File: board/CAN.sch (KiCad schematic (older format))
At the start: 4 parts, among them U401 SN65HVD232

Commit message: - changed some more Vcc labels to +3V3 - combined all input connectors into one big connector - changed can transceiver to MAX3051 - removed HV pin from power connector -> divider now on PS board - updated components - startet layout
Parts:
- removed C401: 2.2u, CRF1:SMD-0603_c, symbol C-RESCUE-BLDC_4
- removed R401: NI, CRF1:SMD-0603_r, symbol R-RESCUE-BLDC_4
- removed R402: 10k, CRF1:SMD-0603_r, symbol R-RESCUE-BLDC_4
- removed U401: SN65HVD232, CRF1:SOIC-8-W, symbol MCP2551-I/SN-RESCUE-BLDC_4
- added C9: 100n, Capacitors_SMD:C_0805, symbol C
- added IC1: MAX3051, Housings_SOIC:SOIC-8_3.9x4.9mm_Pitch1.27mm, symbol MAX3051
- added R3: 120R, Resistors_SMD:R_0805, symbol R
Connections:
- net labels added: +3V3
- net labels removed: VCC
- wire segments 8 -> 4
- no-connect marks 1 -> 0
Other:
- note removed: "Propagation delay\nresistor"

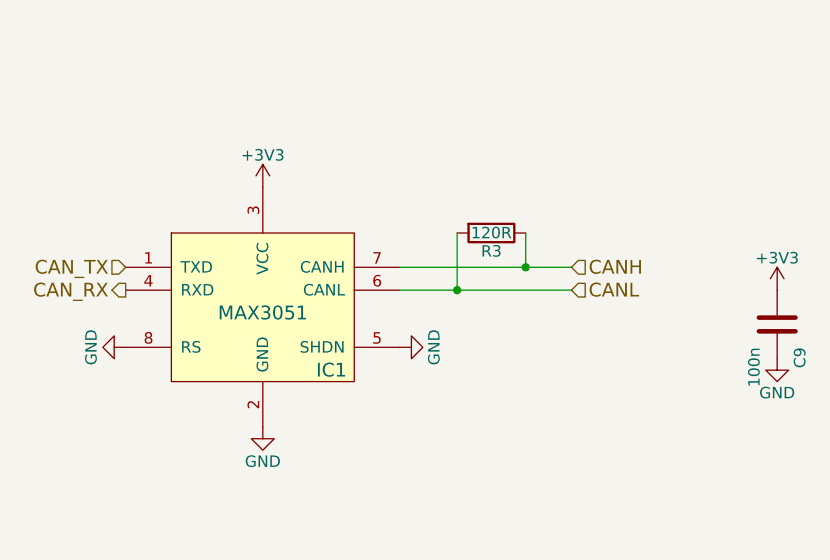
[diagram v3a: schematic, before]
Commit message: - CAN interface isolation
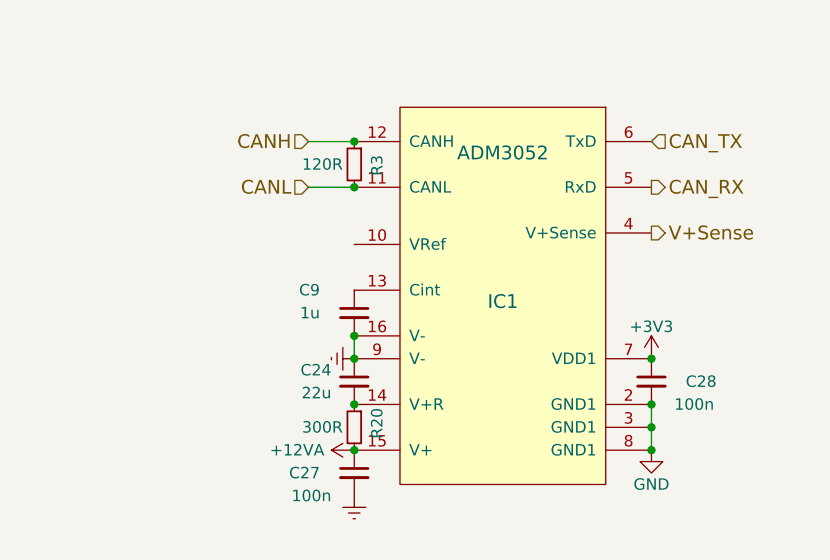
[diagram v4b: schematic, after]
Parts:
- removed C9: 100n, Capacitors_SMD:C_0805, symbol C
- removed IC1: MAX3051, Housings_SOIC:SOIC-8_3.9x4.9mm_Pitch1.27mm, symbol MAX3051
- removed R3: 120R, Resistors_SMD:R_0805, symbol R
- added C24: 22u, Capacitors_SMD:C_0805, symbol C_Small
- added C27, C28: 100n, Capacitors_SMD:C_0805, symbol C_Small
- added C9: 1u, Capacitors_SMD:C_0805, symbol C_Small
- added IC1: ADM3052, Housings_SOIC:SOIC-16_7.5x10.3mm_Pitch1.27mm, symbol ADM3052
- added R20: 300R, Resistors_SMD:R_1206, symbol R_Small
- added R3: 120R, Resistors_SMD:R_0805, symbol R_Small
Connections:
- net +3V3: now also C28.1, IC1.7 (VDD1)
- net CANH: now also IC1.12 (CANH), R3.1
- net CANL: now also IC1.11 (CANL), R3.2
- net CAN_RX: now also IC1.5 (RxD)
- net CAN_TX: now also IC1.6 (TxD)
- net GND: now also C28.2, IC1.2 (GND1), IC1.3 (GND1), IC1.8 (GND1)
- new net: C9.1, IC1.13 (Cint)
- new net: C24.2, IC1.14 (V+R), R20.1
- new net +12VA: C27.1, IC1.15 (V+), R20.2
- new net Earth: C24.1, C27.2, C9.2, IC1.16 (V-), IC1.9 (V-)
- new net V+Sense: IC1.4 (V+Sense)
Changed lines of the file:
@@
 Comment4 ""
 $EndDescr
-Text HLabel 4350 3800 0    60   Output ~ 0
+Text HLabel 6650 3350 2    60   Output ~ 0
 CAN_RX
-Text HLabel 4350 3700 0    60   Input ~ 0
+Text HLabel 6650 3150 2    60   Input ~ 0
 CAN_TX
-Text HLabel 6300 3700 2    60   Input ~ 0
+Text HLabel 5150 3150 0    60   Input ~ 0
 CANH
-Text HLabel 6300 3800 2    60   Input ~ 0
+Text HLabel 5150 3350 0    60   Input ~ 0
 CANL
 $Comp
-L MAX3051 IC1
-U 1 1 57560849
-P 4950 3800
-F 0 "IC1" H 5250 3450 60  0000 C CNN
-F 1 "MAX3051" H 4950 3700 60  0000 C CNN
-F 2 "Housings_SOIC:SOIC-8_3.9x4.9mm_Pitch1.27mm" H 4950 3800 60  0001 C CNN
-F 3 "" H 4950 3800 60  0000 C CNN
-	1    4950 3800
+L ADM3052 IC1
+U 1 1 5759CEA3
+P 6000 3850
+F 0 "IC1" H 6000 3850 60  0000 C CNN
+F 1 "ADM3052" H 6000 4500 60  0000 C CNN
+F 2 "Housings_SOIC:SOIC-16_7.5x10.3mm_Pitch1.27mm" H 6150 3950 60  0001 C CNN
+F 3 "" H 6150 3950 60  0000 C CNN
+	1    6000 3850
+	-1   0    0    -1
+$EndComp
+$Comp
+L C_Small C9
+U 1 1 5759CF39
+P 5350 3900
+F 0 "C9" H 5500 4000 50  0000 L CNN
+F 1 "1u" H 5500 3900 50  0000 L CNN
+F 2 "Capacitors_SMD:C_0805" H 5350 3900 60  0001 C CNN
+F 3 "" H 5350 3900 60  0000 C CNN
+	1    5350 3900
+	-1   0    0    -1
+$EndComp
+$Comp
+L C_Small C24
+U 1 1 5759CF9E
+P 5350 4200
+F 0 "C24" H 5450 4250 50  0000 L CNN
+F 1 "22u" H 5450 4150 50  0000 L CNN
+F 2 "Capacitors_SMD:C_0805" H 5350 4200 60  0001 C CNN
+F 3 "" H 5350 4200 60  0000 C CNN
+	1    5350 4200
+	-1   0    0    -1
+$EndComp
+Connection ~ 5350 4100
+Connection ~ 5350 4300
+$Comp
+L R_Small R20
+U 1 1 5759CFE0
+P 5350 4400
+F 0 "R20" V 5250 4350 50  0000 L CNN
+F 1 "300R" H 5400 4400 50  0000 L CNN
+F 2 "Resistors_SMD:R_1206" H 5350 4400 60  0001 C CNN
+F 3 "" H 5350 4400 60  0000 C CNN
+	1    5350 4400
+	-1   0    0    -1
+$EndComp
+$Comp
+L C_Small C27
+U 1 1 5759D08A
+P 5350 4600
+F 0 "C27" H 5500 4600 50  0000 L CNN
+F 1 "100n" H 5450 4500 50  0000 L CNN
+F 2 "Capacitors_SMD:C_0805" H 5350 4600 60  0001 C CNN
+F 3 "" H 5350 4600 60  0000 C CNN
+	1    5350 4600
+	-1   0    0    -1
+$EndComp
+Connection ~ 5350 4500
+$Comp
+L Earth #PWR046
+U 1 1 5759DCFE
+P 5350 4700
+F 0 "#PWR046" H 5350 4450 50  0001 C CNN
+F 1 "Earth" H 5350 4550 50  0001 C CNN
+F 2 "" H 5350 4700 60  0000 C CNN
+F 3 "" H 5350 4700 60  0000 C CNN
+	1    5350 4700
+	-1   0    0    -1
+$EndComp
+$Comp
+L Earth #PWR047
+U 1 1 5759DF52
+P 5350 4100
+F 0 "#PWR047" H 5350 3850 50  0001 C CNN
+F 1 "Earth" H 5350 3950 50  0001 C CNN
+F 2 "" H 5350 4100 60  0000 C CNN
+F 3 "" H 5350 4100 60  0000 C CNN
+	1    5350 4100
+	0    1    -1   0
+$EndComp
+$Comp
+L +12VA #PWR048
+U 1 1 5759E22F
+P 5350 4500
+F 0 "#PWR048" H 5350 4350 50  0001 C CNN
+F 1 "+12VA" V 5350 4750 50  0000 C CNN
+F 2 "" H 5350 4500 60  0000 C CNN
+F 3 "" H 5350 4500 60  0000 C CNN
+	1    5350 4500
+	0    -1   -1   0
+$EndComp
+$Comp
+L GND #PWR049
+U 1 1 5759E8F5
+P 6650 4500
+F 0 "#PWR049" H 6650 4250 50  0001 C CNN
+F 1 "GND" H 6650 4350 50  0000 C CNN
+F 2 "" H 6650 4500 60  0000 C CNN
+F 3 "" H 6650 4500 60  0000 C CNN
+	1    6650 4500
 	1    0    0    -1
 $EndComp
 $Comp
-L +3V3 #PWR046
-U 1 1 57560949
-P 4950 3350
-F 0 "#PWR046" H 4950 3200 50  0001 C CNN
-F 1 "+3V3" H 4950 3490 50  0000 C CNN
-F 2 "" H 4950 3350 60  0000 C CNN
-F 3 "" H 4950 3350 60  0000 C CNN
-	1    4950 3350
+L R_Small R3
+U 1 1 5759ED7A
+P 5350 3250
+F 0 "R3" V 5250 3200 50  0000 L CNN
+F 1 "120R" H 5400 3250 50  0000 L CNN
+F 2 "Resistors_SMD:R_0805" H 5350 3250 60  0001 C CNN
+F 3 "" H 5350 3250 60  0000 C CNN
+	1    5350 3250
+	-1   0    0    -1
+$EndComp
+Wire Wire Line
+	5150 3350 5350 3350
+Wire Wire Line
+	5350 3150 5150 3150
+Connection ~ 5350 3150
+Connection ~ 5350 3350
+Text HLabel 6650 3550 2    60   Output ~ 0
+V+Sense
+$Comp
+L C_Small C28
+U 1 1 575A0498
+P 6650 4200
+F 0 "C28" H 6800 4200 50  0000 L CNN
+F 1 "100n" H 6750 4100 50  0000 L CNN
+F 2 "Capacitors_SMD:C_0805" H 6650 4200 60  0001 C CNN
+F 3 "" H 6650 4200 60  0000 C CNN
+	1    6650 4200
 	1    0    0    -1
 $EndComp
+Connection ~ 6650 4300
+Connection ~ 6650 4500
 $Comp
-L C C9
-U 1 1 5756096A
-P 7200 3950
-F 0 "C9" V 7300 4050 50  0000 L CNN
-F 1 "100n" V 7100 4050 50  0000 L CNN
-F 2 "Capacitors_SMD:C_0805" H 7238 3800 30  0001 C CNN
-F 3 "" H 7200 3950 60  0000 C CNN
-	1    7200 3950
-	1    0    0    1
-$EndComp
-$Comp
-L GND #PWR047
-U 1 1 57560A1D
-P 7200 4100
-F 0 "#PWR047" H 7200 3850 50  0001 C CNN
-F 1 "GND" H 7200 3950 50  0000 C CNN
-F 2 "" H 7200 4100 60  0000 C CNN
-F 3 "" H 7200 4100 60  0000 C CNN
-	1    7200 4100
+L +3V3 #PWR050
+U 1 1 575A0BC8
+P 6650 4100
+F 0 "#PWR050" H 6650 3950 50  0001 C CNN
+F 1 "+3V3" H 6650 4240 50  0000 C CNN
+F 2 "" H 6650 4100 60  0000 C CNN
+F 3 "" H 6650 4100 60  0000 C CNN
+	1    6650 4100
 	1    0    0    -1
 $EndComp
-$Comp
-L +3V3 #PWR048
-U 1 1 57560AF4
-P 7200 3800
-F 0 "#PWR048" H 7200 3650 50  0001 C CNN
-F 1 "+3V3" H 7200 3940 50  0000 C CNN
-F 2 "" H 7200 3800 60  0000 C CNN
-F 3 "" H 7200 3800 60  0000 C CNN
-	1    7200 3800
-	1    0    0    -1
-$EndComp
-$Comp
-L R R3
-U 1 1 57560DD5
-P 5950 3550
-F 0 "R3" V 6030 3550 50  0000 C CNN
-F 1 "120R" V 5950 3550 50  0000 C CNN
-F 2 "Resistors_SMD:R_0805" V 5880 3550 30  0001 C CNN
-F 3 "" H 5950 3550 30  0000 C CNN
-	1    5950 3550
-	0    1    1    0
-$EndComp
 Wire Wire Line
-	5800 3550 5800 3800
+	6650 4300 6650 4500
+Connection ~ 6650 4400
 Wire Wire Line
-	5550 3800 6300 3800
-Wire Wire Line
-	5550 3700 6300 3700
-Wire Wire Line
-	6100 3700 6100 3550
-Connection ~ 6100 3700
-Connection ~ 5800 3800
-$Comp
-L GND #PWR049
-U 1 1 57561094
-P 4950 4400
-F 0 "#PWR049" H 4950 4150 50  0001 C CNN
-F 1 "GND" H 4950 4250 50  0000 C CNN
-F 2 "" H 4950 4400 60  0000 C CNN
-F 3 "" H 4950 4400 60  0000 C CNN
-	1    4950 4400
-	1    0    0    -1
-$EndComp
-$Comp
-L GND #PWR050
-U 1 1 575615AF
-P 5550 4050
-F 0 "#PWR050" H 5550 3800 50  0001 C CNN
-F 1 "GND" H 5550 3900 50  0000 C CNN
-F 2 "" H 5550 4050 60  0000 C CNN
-F 3 "" H 5550 4050 60  0000 C CNN
-	1    5550 4050
-	0    -1   -1   0
-$EndComp
-$Comp
-L GND #PWR051
-U 1 1 575615C3
-P 4350 4050
-F 0 "#PWR051" H 4350 3800 50  0001 C CNN
-F 1 "GND" H 4350 3900 50  0000 C CNN
-F 2 "" H 4350 4050 60  0000 C CNN
-F 3 "" H 4350 4050 60  0000 C CNN
-	1    4350 4050
-	0    1    1    0
-$EndComp
+	5350 4000 5350 4100
+Connection ~ 5350 4000
+Connection ~ 6650 4100
 $EndSCHEMATC
